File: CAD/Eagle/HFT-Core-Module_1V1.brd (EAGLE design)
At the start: 96.5 x 96.5 mm, 402 parts, among them Q0521 ABS07-32.768KHZ, Q0811 ABM03B-32.000MHZ, Q0911 ABM3B-16MHZ-10-R50-1-U, T1201 MMBT2222, T1202 MMBT2222, T1203 MMBT2222, U0111 STM32L4Z_144PIN_SMPS, U0431 PAM2305AAB120, U0601 LM4120IM5-3.0, U0611 MAX5217, U0631 CFPT-141-20MHZ, U0641 OPA354, U0701 Si5338, U0801 SX1276, U0901 AX5243, U0911 PE4259, U0921 PE4259, U0991 PE4259, U1101 MCP3911A0-E-SS, U1111 MAX5136AGTG+, U1121 OPA354, U1131 OPA354, U1141 OPA354, U1201 NHD-C0220BIZ_2X20CHARS, U1301 MPU-9250, U1311 MS5607-02BA03, U1321 SHT31-DIS, U1402 SPV1040T, U1501 TS5A23166, U1601 SC189ZSKTRT, U1701 TS5A23166, U1801 TS5A23166, U1901 TS5A23166, X1261 TTE_EN11-HSM, X1401 WIRE-TO-BOARD_5MM08_1X02, X2001 MOLEX 105017-0001, X2101 SMA_SMT_AMPHENOL-901-143, SAM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, X2111 SMA_SMT_AMPHENOL-901-143, SAM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, X2201 CUI SJ1-3535NS, X2211 CUI SJ1-3535NS, X2311 2X20/90_1MM27_HARWIN_M50-3202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, X2312 2X20/90_1MM27_HARWIN_M50-3202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, X2321 2X20/90_1MM27_HARWIN_M50-3202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, X2322 2X20/90_1MM27_HARWIN_M50-3202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, X2331 2X20/90_1MM27_HARWIN_M50-3202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, X2332 2X20/90_1MM27_HARWIN_M50-3202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

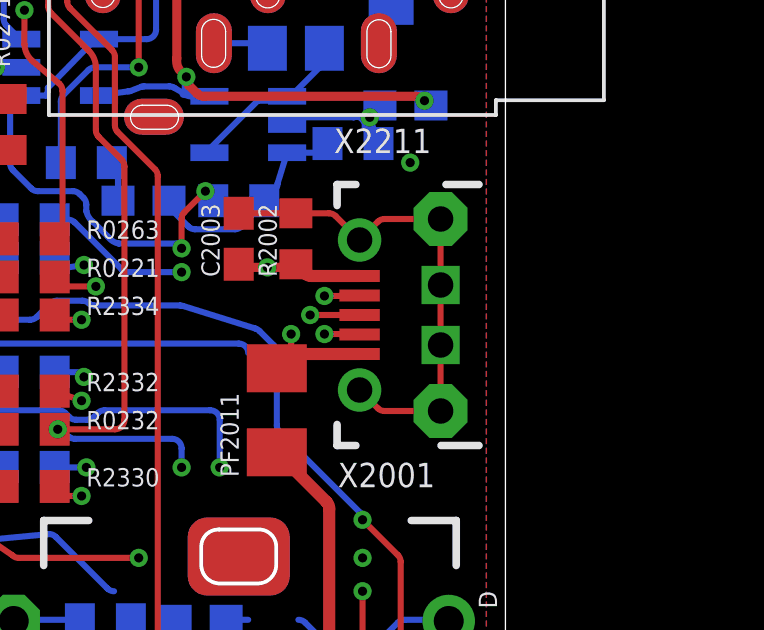
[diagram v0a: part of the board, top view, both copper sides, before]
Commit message: HW_1V1 - CAD/Eagle - Micro-USB receptacle corrected
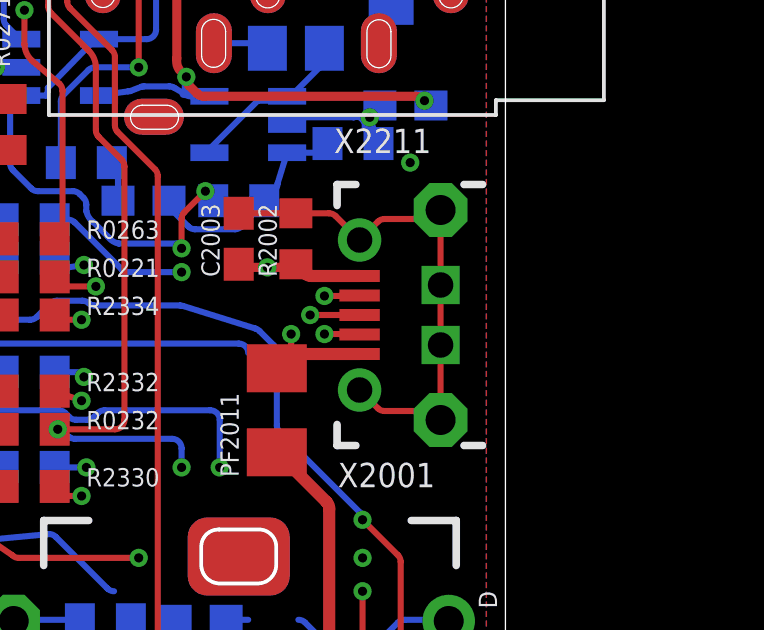
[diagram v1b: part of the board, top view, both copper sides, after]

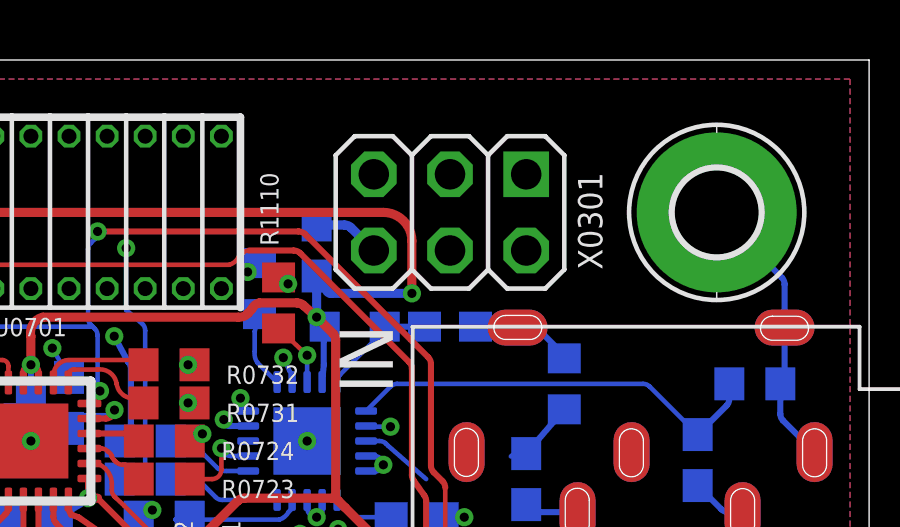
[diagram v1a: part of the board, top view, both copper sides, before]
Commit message: HW_1V1 - CAD/Eagle - programmer socket changed, Reset button is of type NO and not NC
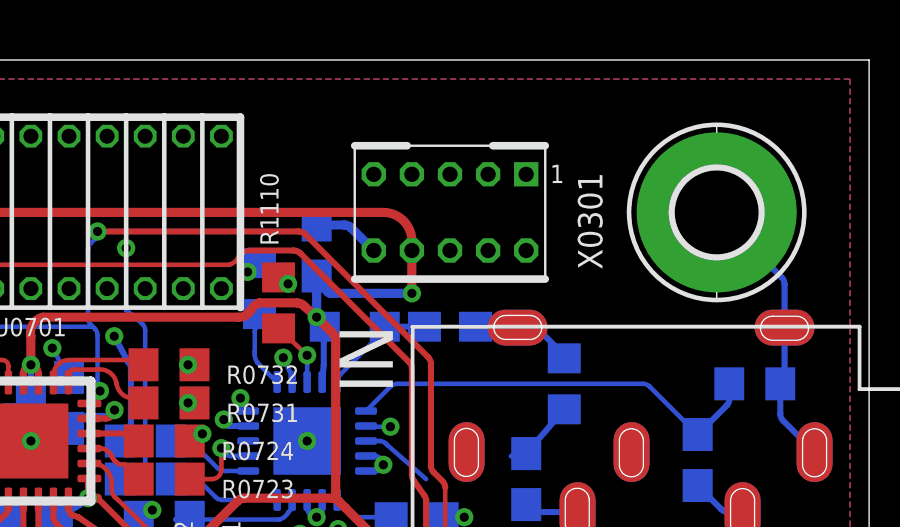
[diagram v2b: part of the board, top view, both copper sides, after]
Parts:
- R1201: value 1.8kR -> 2.0kR
- R1202: value 5.2kR -> 1.5kR
- R1203: value 68R -> 27R
- S0312: value KSR223G -> KSR223GLFG
- X0301: device df4iah_connector:2X03 -> df4iah_connector:2X05_SHROUDED_1MM27
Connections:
- net +3V3: now also X0301.1; no longer X0301.2
- net GND: now also X0301.3, X0301.5, X0301.9; no longer X0301.6
- net MCU_NRST: now also X0301.10
- net PA13: now also X0301.2; no longer X0301.1
- net PA14: now also X0301.4; no longer X0301.5
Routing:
- net PA13: track 27.7 -> 25.8 mm

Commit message: HW_1V1 - CAD/Eagle - first round of new routing done
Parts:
- moved X0301 2.08 mm to (84.2, 92.7)
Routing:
- net MCU_NRST: track 16.9 -> 98.5 mm, vias 2 -> 6
- net VSOL: track 48.4 -> 84.5 mm, vias 3 -> 6
- net PW00: track 54.5 -> 76.4 mm
- net +5V0: track 224.8 -> 245.3 mm, vias 3 -> 2
- net UART1_RX_IN: track 61.7 -> 81.0 mm
- net AX_16MHZ: track 84.5 -> 102.2 mm
- net PD12: track 162.3 -> 179.1 mm, vias 6 -> 8
- net GND: track 277.8 -> 289.5 mm
- net MCU_I2C4_SDA: track 216.6 -> 227.7 mm
- net PD8: track 87.3 -> 96.2 mm
- net I2S_MCLK_OUT: track 215.1 -> 223.0 mm
- net PA14: track 26.5 -> 33.0 mm
- net PW01: track 77.9 -> 84.3 mm
- net PG3: track 73.6 -> 80.0 mm, vias 2 -> 3
- net I2S_SD_OUT: track 215.7 -> 220.9 mm
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
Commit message: HW_1V1 - CAD/Eagle - second round done
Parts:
- moved C1132 0.86 mm to (91.9, 73.4), turned to 180 degrees
- moved C1129 0.36 mm to (87.6, 78.7)
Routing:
- net MCU_VBAT: track 23.3 -> 43.0 mm, vias 2 -> 3
- net +3V3: track 135.0 -> 150.5 mm, vias 27 -> 30
- net UART1_TX_OUT: track 64.6 -> 76.3 mm
- net MCP3911_CH1+: track 4.94 -> 9.36 mm
- net AUDIO_OUT_L_OP: track 5.41 -> 6.95 mm
- net AUDIO_OUT_L: track 1.41 -> 2.27 mm
- net PA13: track 25.5 -> 26.3 mm
- net GND: track 289.5 -> 289.8 mm, vias 127 -> 130

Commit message: HW_1V1 - SWD header, XO 32.768kHz caps, RESET resistor removed, SWD resistors added
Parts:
- removed R0311: 3.3kR, rcl:R0603
- added C0532: 12pF, rcl:C0603
- added R0331, R0332: 100kR, rcl:R0603
- C0511: value 1.5pF -> 18pF
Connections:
- net +3V3: now also R0331.2, X0322.1; no longer R0311.1, R0321.1
- net GND: now also C0532.2, R0321.1, R0332.1; no longer X0322.2
- net MCU_NRST: no longer R0311.2
- net PA13: now also R0331.1
- net PA14: now also R0332.2
- net PC14_MCU_OSC32_IN: now also C0532.1
- net PH3_BOOT0: now also X0322.2; no longer X0322.1
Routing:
- net PH3_BOOT0: track 11.9 -> 9.00 mm
- net MCU_NRST: track 98.5 -> 96.6 mm
- net +3V3: track 150.5 -> 149.6 mm, vias 30 -> 29
- net GND: track 289.8 -> 288.9 mm

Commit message: HW_1V1 - LCD-backlight resistors changed
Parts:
- R1204, R1207: value 2.2kR -> 2.0kR
- R1205, R1208: value 1.8kR -> 1.5kR
- R1206, R1209: value 10R -> 27R
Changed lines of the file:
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@@
 <attribute name="VALUE" x="20.32" y="17.145" size="0.6096" layer="28" font="vector" ratio="10" rot="MR270"/>
 </element>
-<element name="R1209" library="rcl" package="R0805" value="10R" x="21.59" y="14.605" smashed="yes" rot="MR0">
+<element name="R1209" library="rcl" package="R0805" value="27R" x="21.59" y="14.605" smashed="yes" rot="MR0">
 <attribute name="NAME" x="26.035" y="14.2875" size="0.6096" layer="26" font="vector" ratio="10" rot="MR0"/>
 <attribute name="VALUE" x="22.225" y="12.065" size="0.6096" layer="28" font="vector" ratio="10" rot="MR0"/>
 </element>
-<element name="R1208" library="rcl" package="R0603" value="1.8kR" x="21.59" y="16.51" smashed="yes" rot="MR0">
+<element name="R1208" library="rcl" package="R0603" value="1.5kR" x="21.59" y="16.51" smashed="yes" rot="MR0">
 <attribute name="NAME" x="26.035" y="16.1925" size="0.6096" layer="26" font="vector" ratio="10" rot="MR0"/>
 <attribute name="VALUE" x="22.225" y="14.605" size="0.6096" layer="28" font="vector" ratio="10" rot="MR0"/>
 </element>
-<element name="R1207" library="rcl" package="R0603" value="2.2kR" x="62.23" y="47.625" smashed="yes" rot="MR90">
+<element name="R1207" library="rcl" package="R0603" value="2.0kR" x="62.23" y="47.625" smashed="yes" rot="MR90">
 <attribute name="NAME" x="61.9125" y="43.18" size="0.6096" layer="26" font="vector" ratio="10" rot="MR90"/>
 <attribute name="VALUE" x="60.325" y="46.99" size="0.6096" layer="28" font="vector" ratio="10" rot="MR90"/>
 </element>
-<element name="R1206" library="rcl" package="R0805" value="10R" x="21.59" y="18.415" smashed="yes" rot="MR0">
+<element name="R1206" library="rcl" package="R0805" value="27R" x="21.59" y="18.415" smashed="yes" rot="MR0">
 <attribute name="NAME" x="26.035" y="18.0975" size="0.6096" layer="26" font="vector" ratio="10" rot="MR0"/>
 <attribute name="VALUE" x="22.225" y="15.875" size="0.6096" layer="28" font="vector" ratio="10" rot="MR0"/>
@@
 <attribute name="VALUE" x="22.225" y="19.685" size="0.6096" layer="28" font="vector" ratio="10" rot="MR0"/>
 </element>
-<element name="R1205" library="rcl" package="R0603" value="1.8kR" x="21.59" y="20.32" smashed="yes" rot="MR0">
+<element name="R1205" library="rcl" package="R0603" value="1.5kR" x="21.59" y="20.32" smashed="yes" rot="MR0">
 <attribute name="NAME" x="26.035" y="20.0025" size="0.6096" layer="26" font="vector" ratio="10" rot="MR0"/>
 <attribute name="VALUE" x="22.225" y="18.415" size="0.6096" layer="28" font="vector" ratio="10" rot="MR0"/>
@@
 <attribute name="VALUE" x="22.225" y="22.225" size="0.6096" layer="28" font="vector" ratio="10" rot="MR0"/>
 </element>
-<element name="R1204" library="rcl" package="R0603" value="2.2kR" x="59.055" y="47.625" smashed="yes" rot="R90">
+<element name="R1204" library="rcl" package="R0603" value="2.0kR" x="59.055" y="47.625" smashed="yes" rot="R90">
 <attribute name="NAME" x="59.055" y="43.18" size="0.6096" layer="25" font="vector" ratio="10" rot="R90"/>
 <attribute name="VALUE" x="60.96" y="46.99" size="0.6096" layer="27" font="vector" ratio="10" rot="R90"/>

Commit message: HW_1V1 - I2C addresses changed, LCD will be replaced by EA DOGS104N-A
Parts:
- R1331, R1332: value 3.9kR -> 1.0kR
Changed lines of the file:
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@@
 <attribute name="VALUE" x="43.18" y="26.67" size="0.6096" layer="28" font="vector" ratio="10" rot="MR90"/>
 </element>
-<element name="R1331" library="rcl" package="R0603" value="3.9kR" x="5.715" y="15.875" smashed="yes" rot="MR0">
+<element name="R1331" library="rcl" package="R0603" value="1.0kR" x="5.715" y="15.875" smashed="yes" rot="MR0">
 <attribute name="NAME" x="10.16" y="15.5575" size="0.6096" layer="26" font="vector" ratio="10" rot="MR0"/>
 <attribute name="VALUE" x="6.35" y="13.97" size="0.6096" layer="28" font="vector" ratio="10" rot="MR0"/>
 </element>
-<element name="R1332" library="rcl" package="R0603" value="3.9kR" x="5.715" y="13.335" smashed="yes" rot="MR0">
+<element name="R1332" library="rcl" package="R0603" value="1.0kR" x="5.715" y="13.335" smashed="yes" rot="MR0">
 <attribute name="NAME" x="10.16" y="13.0175" size="0.6096" layer="26" font="vector" ratio="10" rot="MR0"/>
 <attribute name="VALUE" x="6.35" y="11.43" size="0.6096" layer="28" font="vector" ratio="10" rot="MR0"/>

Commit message: HW_1V1 - multiple TODOs for new design added
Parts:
- R0638, R0639: value 50R -> 47R
- R0751: value 100R -> N/A
- R1501: value 50R -> 68R
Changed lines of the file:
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@@
 <attribute name="VALUE" x="69.215" y="79.375" size="0.6096" layer="28" font="vector" ratio="10" rot="MR0"/>
 </element>
-<element name="R0751" library="rcl" package="R0603" value="100R" x="71.12" y="76.120625" smashed="yes" rot="R180">
+<element name="R0751" library="rcl" package="R0603" value="N/A" x="71.12" y="76.120625" smashed="yes" rot="R180">
 <attribute name="NAME" x="69.85" y="74.850625" size="0.6096" layer="25" font="vector" ratio="10"/>
 <attribute name="VALUE" x="71.755" y="78.025625" size="0.6096" layer="27" font="vector" ratio="10" rot="R180"/>
@@
 <attribute name="VALUE" x="73.66" y="78.105" size="0.6096" layer="27" font="vector" ratio="10" rot="R90"/>
 </element>
-<element name="R0638" library="rcl" package="R0603" value="50R" x="55.88" y="80.645" smashed="yes">
+<element name="R0638" library="rcl" package="R0603" value="47R" x="55.88" y="80.645" smashed="yes">
 <attribute name="NAME" x="58.7375" y="80.01" size="0.6096" layer="25" font="vector" ratio="10" rot="R90"/>
 <attribute name="VALUE" x="55.245" y="78.74" size="0.6096" layer="27" font="vector" ratio="10"/>
 </element>
-<element name="R0639" library="rcl" package="R0603" value="50R" x="55.88" y="79.375" smashed="yes">
+<element name="R0639" library="rcl" package="R0603" value="47R" x="55.88" y="79.375" smashed="yes">
 <attribute name="NAME" x="54.2925" y="77.7875" size="0.6096" layer="25" font="vector" ratio="10"/>
 <attribute name="VALUE" x="55.245" y="77.47" size="0.6096" layer="27" font="vector" ratio="10"/>
@@
 </element>
 <element name="X1401" library="df4iah_connector" package="WIRE-TO-BOARD_5MM08_1X02" value="WIRE-TO-BOARD_5MM08_1X02" x="5.08" y="82.55" rot="R180"/>
-<element name="R1501" library="df4iah_rcl" package="R0805" value="50R" x="24.765" y="45.974" smashed="yes" rot="MR90">
+<element name="R1501" library="df4iah_rcl" package="R0805" value="68R" x="24.765" y="45.974" smashed="yes" rot="MR90">
 <attribute name="NAME" x="23.114" y="44.45" size="0.6096" layer="26" font="vector" ratio="10" rot="MR90"/>
 <attribute name="VALUE" x="22.225" y="45.339" size="1.27" layer="28" rot="MR90"/>
